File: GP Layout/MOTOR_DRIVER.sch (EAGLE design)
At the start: 46 parts, among them U2 CSD18502KCS_KCS_3, U3 MIC4604YM, U4 CSD18502KCS_KCS_3, U5 CSD18502KCS_KCS_3, U6 MIC4604YM, U7 ATMEGA328P_TQFP, Y1 16MHz

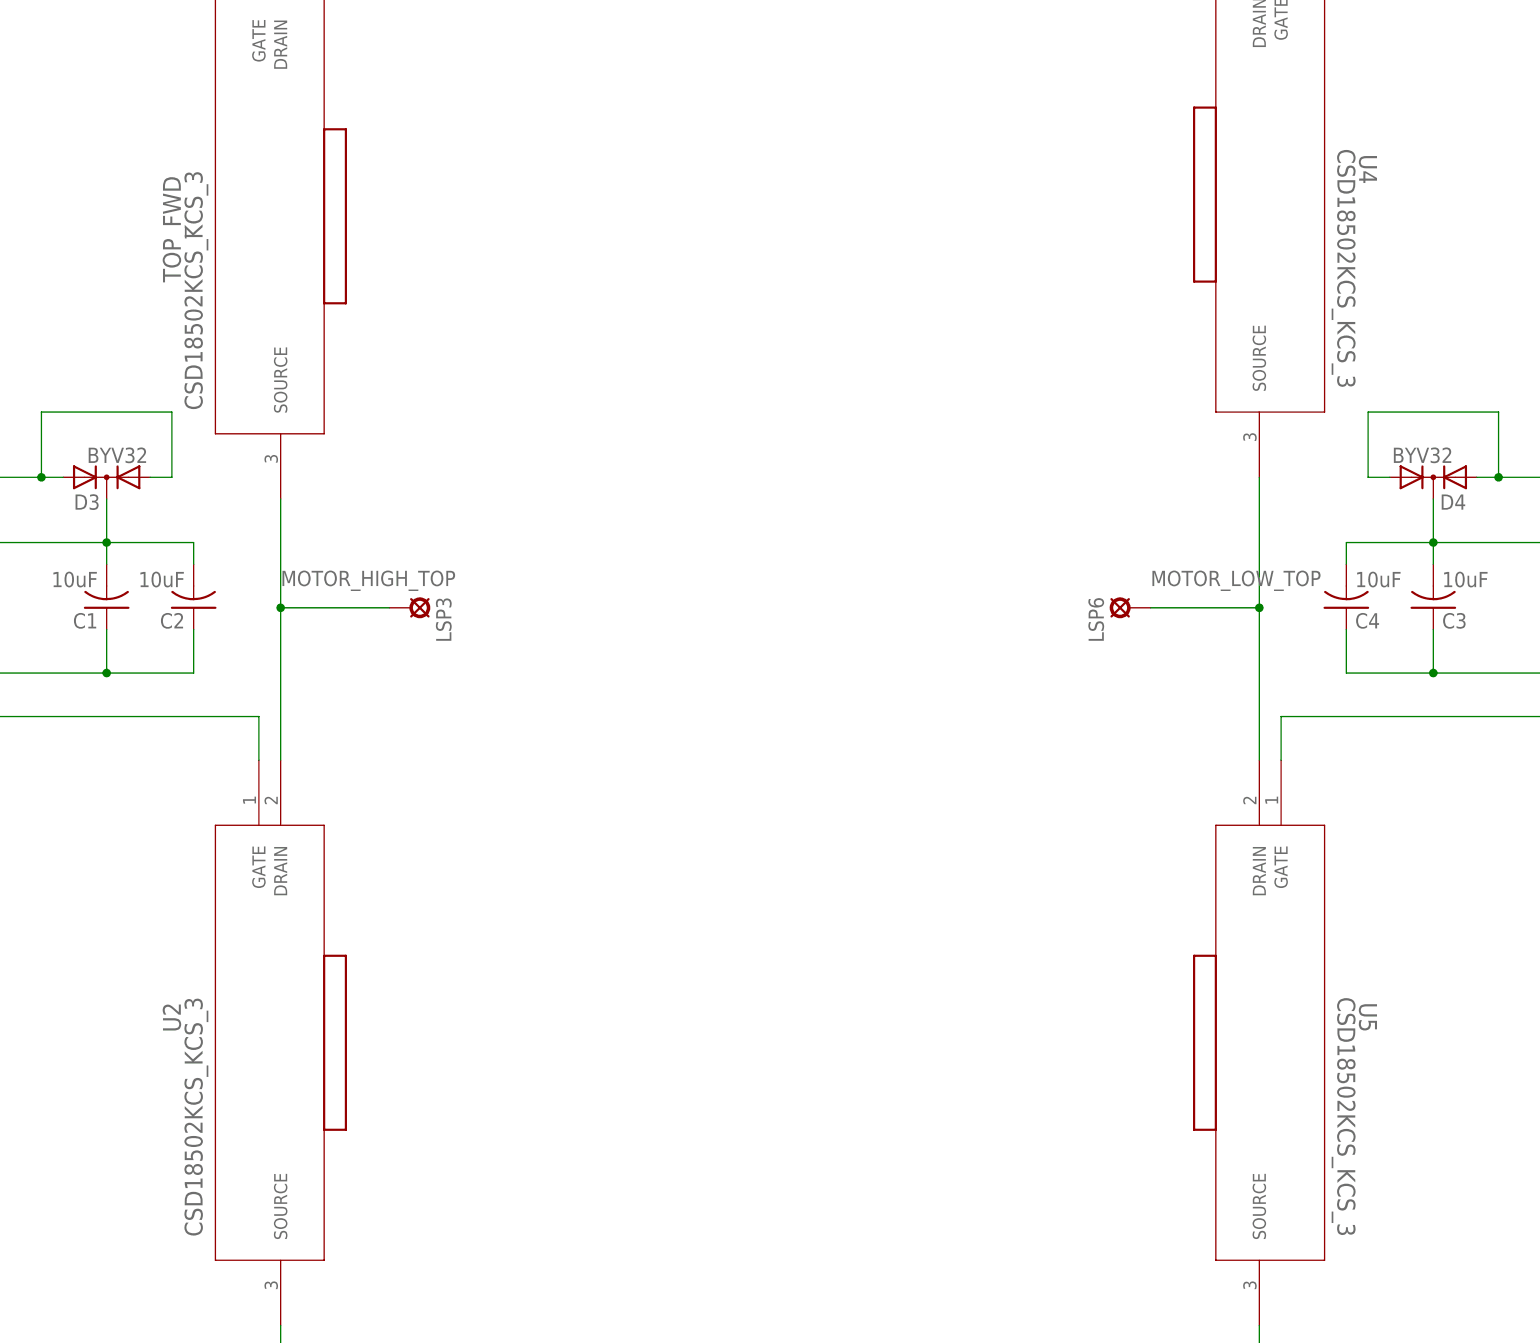
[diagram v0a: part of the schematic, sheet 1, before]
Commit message: modified footprint for MOS to have name and indicate orientation
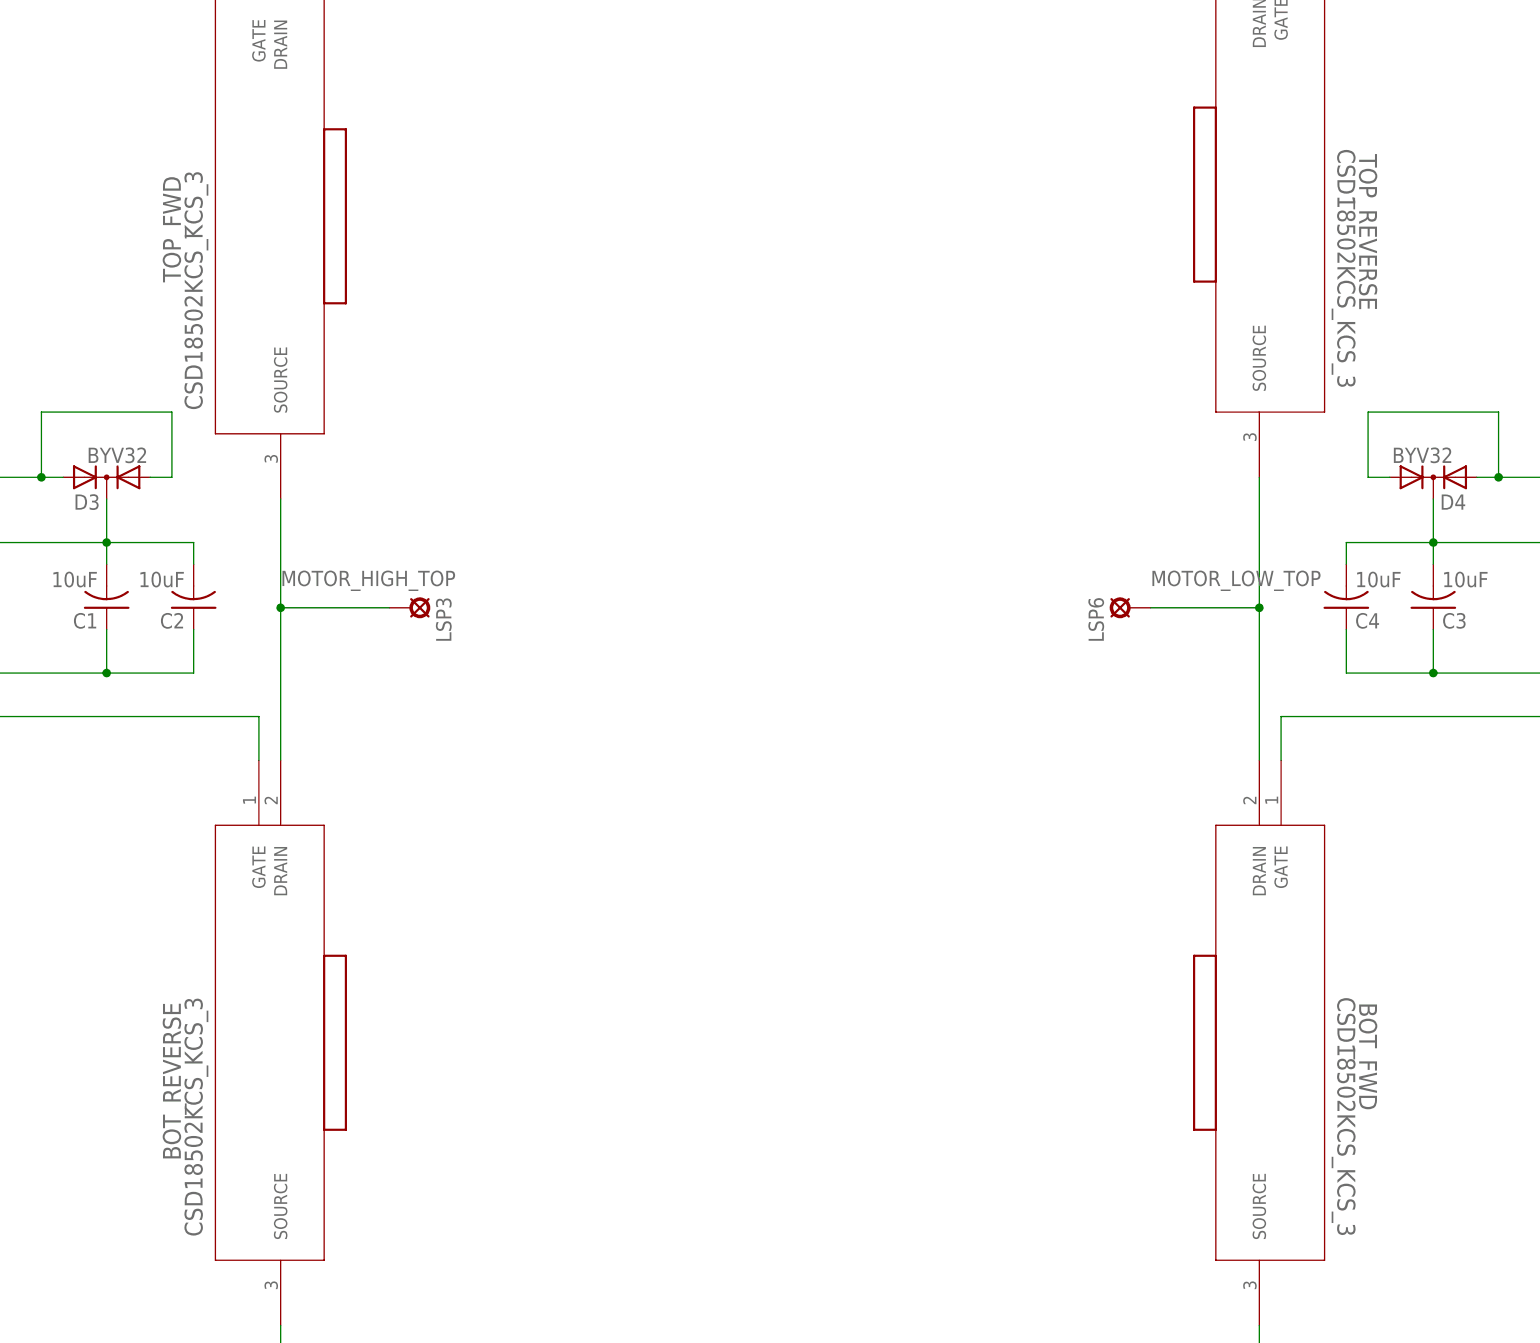
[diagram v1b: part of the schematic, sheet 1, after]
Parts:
- renumbered U2 to BOT_REVERSE, U4 to TOP_REVERSE, U5 to BOT_FWD
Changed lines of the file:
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@@
 <parts>
 <part name="TOP_FWD" library="CSD18502KCS" deviceset="CSD18502KCS_KCS_3" device=""/>
-<part name="U2" library="CSD18502KCS" deviceset="CSD18502KCS_KCS_3" device=""/>
+<part name="BOT_REVERSE" library="CSD18502KCS" deviceset="CSD18502KCS_KCS_3" device=""/>
 <part name="FRAME1" library="frames" deviceset="A3L-LOC" device=""/>
 <part name="U3" library="MIC4604" deviceset="MIC4604YM" device=""/>
@@
 <part name="C2" library="resistor" deviceset="C-US" device="025-050X050" value="10uF"/>
 <part name="LSP3" library="solpad" deviceset="SE14" device=""/>
-<part name="U4" library="CSD18502KCS" deviceset="CSD18502KCS_KCS_3" device=""/>
-<part name="U5" library="CSD18502KCS" deviceset="CSD18502KCS_KCS_3" device=""/>
+<part name="TOP_REVERSE" library="CSD18502KCS" deviceset="CSD18502KCS_KCS_3" device=""/>
+<part name="BOT_FWD" library="CSD18502KCS" deviceset="CSD18502KCS_KCS_3" device=""/>
 <part name="U6" library="MIC4604" deviceset="MIC4604YM" device=""/>
 <part name="C3" library="resistor" deviceset="C-US" device="025-050X050" value="10uF"/>
@@
 <instances>
 <instance part="TOP_FWD" gate="A" x="124.46" y="210.82" rot="MR270"/>
-<instance part="U2" gate="A" x="124.46" y="114.3" rot="MR270"/>
+<instance part="BOT_REVERSE" gate="A" x="124.46" y="114.3" rot="MR270"/>
 <instance part="FRAME1" gate="G$1" x="0" y="0"/>
 <instance part="U3" gate="A" x="86.36" y="142.24" rot="MR0"/>
@@
 <instance part="C2" gate="G$1" x="116.84" y="132.08" rot="R180"/>
 <instance part="LSP3" gate="1" x="142.24" y="132.08" rot="R270"/>
-<instance part="U4" gate="A" x="243.84" y="213.36" rot="R270"/>
-<instance part="U5" gate="A" x="243.84" y="114.3" rot="R270"/>
+<instance part="TOP_REVERSE" gate="A" x="243.84" y="213.36" rot="R270"/>
+<instance part="BOT_FWD" gate="A" x="243.84" y="114.3" rot="R270"/>
 <instance part="U6" gate="A" x="281.94" y="142.24"/>
 <instance part="C3" gate="G$1" x="261.62" y="132.08" rot="MR180"/>
@@
 <wire x1="30.48" y1="142.24" x2="15.24" y2="142.24" width="0.1524" layer="91"/>
 <wire x1="15.24" y1="142.24" x2="15.24" y2="119.38" width="0.1524" layer="91"/>
-<pinref part="U2" gate="A" pin="GATE"/>
+<pinref part="BOT_REVERSE" gate="A" pin="GATE"/>
 <wire x1="15.24" y1="119.38" x2="124.46" y2="119.38" width="0.1524" layer="91"/>
 <wire x1="124.46" y1="119.38" x2="124.46" y2="114.3" width="0.1524" layer="91"/>
@@
 <wire x1="337.82" y1="142.24" x2="353.06" y2="142.24" width="0.1524" layer="91"/>
 <wire x1="353.06" y1="142.24" x2="353.06" y2="119.38" width="0.1524" layer="91"/>
-<pinref part="U5" gate="A" pin="GATE"/>
+<pinref part="BOT_FWD" gate="A" pin="GATE"/>
 <wire x1="353.06" y1="119.38" x2="243.84" y2="119.38" width="0.1524" layer="91"/>
 <wire x1="243.84" y1="119.38" x2="243.84" y2="114.3" width="0.1524" layer="91"/>
@@
 <net name="N$10" class="0">
 <segment>
-<pinref part="U4" gate="A" pin="GATE"/>
+<pinref part="TOP_REVERSE" gate="A" pin="GATE"/>
 <wire x1="243.84" y1="213.36" x2="243.84" y2="218.44" width="0.1524" layer="91"/>
 <wire x1="243.84" y1="218.44" x2="279.4" y2="218.44" width="0.1524" layer="91"/>
@@
 <net name="GND_TOP" class="0">
 <segment>
-<pinref part="U2" gate="A" pin="SOURCE"/>
+<pinref part="BOT_REVERSE" gate="A" pin="SOURCE"/>
 <wire x1="127" y1="48.26" x2="127" y2="40.64" width="0.1524" layer="91"/>
 <pinref part="U3" gate="A" pin="VSS"/>
@@
 <wire x1="12.7" y1="40.64" x2="127" y2="40.64" width="0.1524" layer="91"/>
 <junction x="127" y="40.64"/>
-<pinref part="U5" gate="A" pin="SOURCE"/>
+<pinref part="BOT_FWD" gate="A" pin="SOURCE"/>
 <wire x1="241.3" y1="48.26" x2="241.3" y2="40.64" width="0.1524" layer="91"/>
 <pinref part="U6" gate="A" pin="VSS"/>
@@
 <junction x="127" y="220.98"/>
 <pinref part="U3" gate="A" pin="VDD"/>
-<pinref part="U4" gate="A" pin="DRAIN"/>
+<pinref part="TOP_REVERSE" gate="A" pin="DRAIN"/>
 <wire x1="86.36" y1="147.32" x2="86.36" y2="142.24" width="0.1524" layer="91"/>
 <wire x1="241.3" y1="220.98" x2="241.3" y2="213.36" width="0.1524" layer="91"/>
@@
 <segment>
 <pinref part="TOP_FWD" gate="A" pin="SOURCE"/>
-<pinref part="U2" gate="A" pin="DRAIN"/>
+<pinref part="BOT_REVERSE" gate="A" pin="DRAIN"/>
 <wire x1="127" y1="144.78" x2="127" y2="132.08" width="0.1524" layer="91"/>
 <pinref part="LSP3" gate="1" pin="MP"/>
@@
 <net name="MOTOR_LOW_TOP" class="0">
 <segment>
-<pinref part="U4" gate="A" pin="SOURCE"/>
-<pinref part="U5" gate="A" pin="DRAIN"/>
+<pinref part="TOP_REVERSE" gate="A" pin="SOURCE"/>
+<pinref part="BOT_FWD" gate="A" pin="DRAIN"/>
 <wire x1="241.3" y1="147.32" x2="241.3" y2="132.08" width="0.1524" layer="91"/>
 <pinref part="LSP6" gate="1" pin="MP"/>

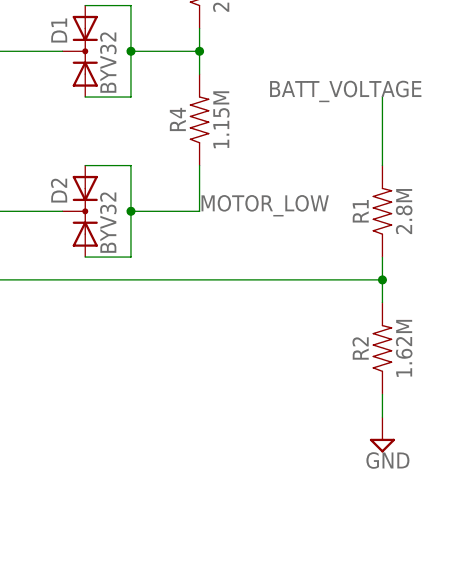
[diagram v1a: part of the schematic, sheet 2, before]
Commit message: Changed battery sense resistances
Input impedance might be too high for the Teensy ADC
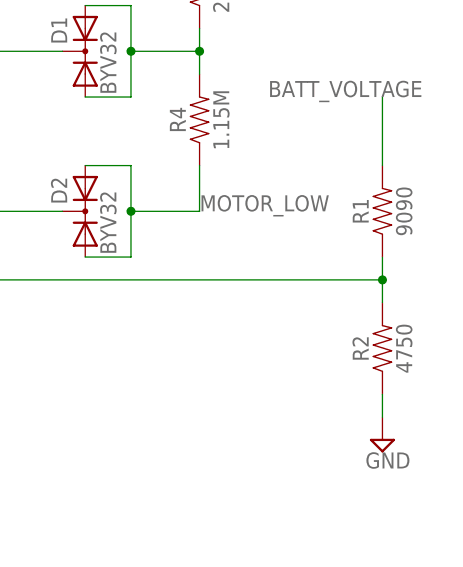
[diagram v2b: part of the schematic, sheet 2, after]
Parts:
- R1: value 2.8M -> 9090
- R2: value 1.62M -> 4750
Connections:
- net 5V: now also SV1.8
- net GND: now also SV1.10
- net SERVO: now also SV1.9
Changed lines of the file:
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@@
 <?xml version="1.0" encoding="utf-8"?>
 <!DOCTYPE eagle SYSTEM "eagle.dtd">
-<eagle version="8.0.1">
+<eagle version="8.0.0">
 <drawing>
 <settings>
@@
 <part name="FUSE" library="minifuse" deviceset="FUSEHOLDER3588" device=""/>
 <part name="BIG_SWITCH" library="bigswitch" deviceset="BIGSWITCH" device=""/>
-<part name="R1" library="SparkFun-Resistors" deviceset="0.3OHM" device="-0805-1/8W-1%" value="2.8M"/>
-<part name="R2" library="SparkFun-Resistors" deviceset="0.3OHM" device="-0805-1/8W-1%" value="1.62M"/>
+<part name="R1" library="SparkFun-Resistors" deviceset="0.3OHM" device="-0805-1/8W-1%" value="9090"/>
+<part name="R2" library="SparkFun-Resistors" deviceset="0.3OHM" device="-0805-1/8W-1%" value="4750"/>
 <part name="SUPPLY2" library="supply2" deviceset="GND" device=""/>
 <part name="R3" library="SparkFun-Resistors" deviceset="0.3OHM" device="-0805-1/8W-1%" value="2.32M"/>
@@
 <wire x1="55.88" y1="157.48" x2="81.28" y2="157.48" width="0.1524" layer="91"/>
 <label x="76.2" y="157.48" size="1.778" layer="95"/>
+<pinref part="SV1" gate="G$1" pin="10"/>
 </segment>
 <segment>
@@
 <wire x1="55.88" y1="152.4" x2="81.28" y2="152.4" width="0.1524" layer="91"/>
 <label x="76.2" y="152.4" size="1.778" layer="95"/>
+<pinref part="SV1" gate="G$1" pin="8"/>
 </segment>
 <segment>
@@
 <wire x1="55.88" y1="154.94" x2="81.28" y2="154.94" width="0.1524" layer="91"/>
 <label x="73.66" y="154.94" size="1.778" layer="95"/>
-</segment>
-</net>
+<pinref part="SV1" gate="G$1" pin="9"/>
+</segment>
+</net>

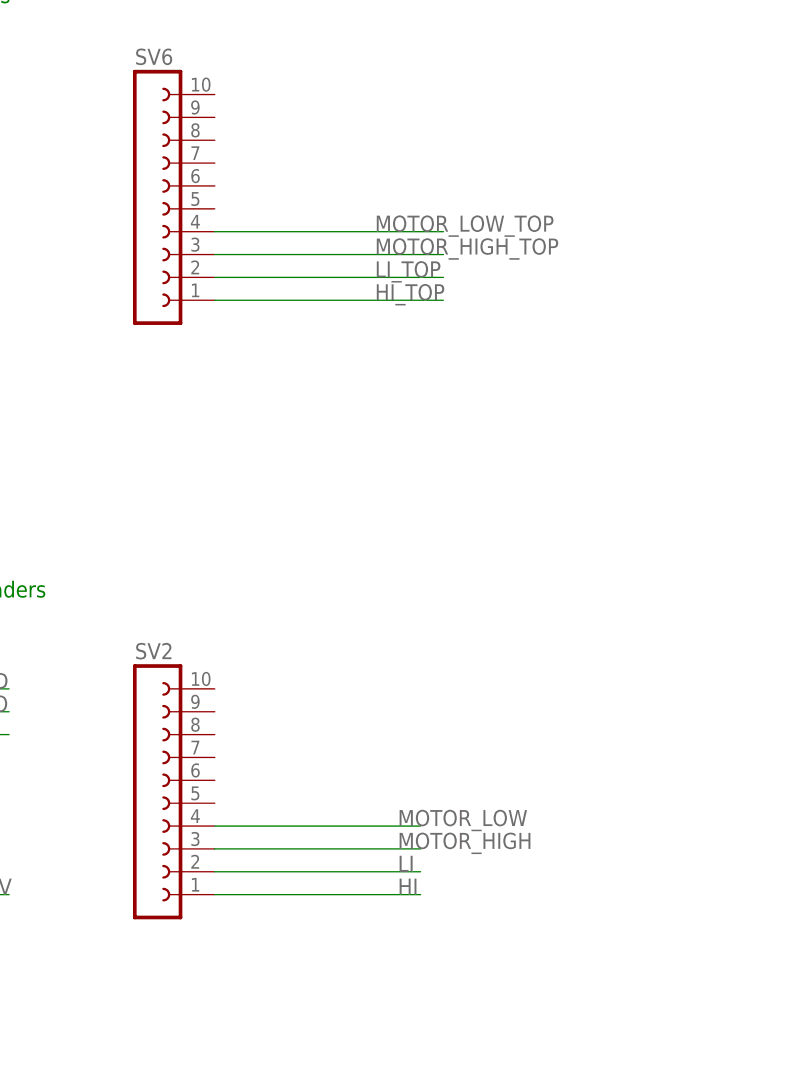
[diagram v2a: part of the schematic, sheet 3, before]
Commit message: added motor inputs for full bridge
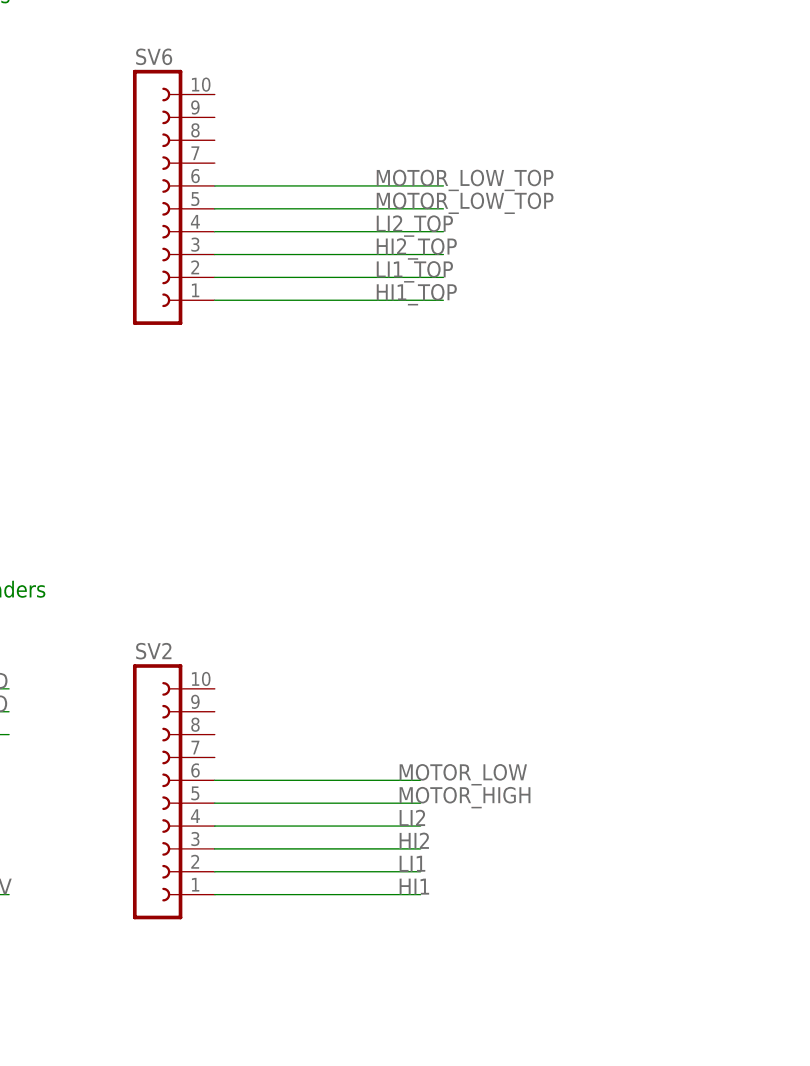
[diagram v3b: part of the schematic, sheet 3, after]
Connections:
- net HI renamed HI1
- net LI renamed LI1
- new net HI1_TOP: SV6.1, U3.HI
- new net HI2: SV2.3, U$1.5
- new net HI2_TOP: SV6.3
- new net LI1_TOP: SV6.2, U3.LI
- new net LI2: SV2.4, U$1.6
- new net LI2_TOP: SV6.4
- net HI_TOP: no longer SV6.1, U3.HI
- net LI_TOP: no longer SV6.2, U3.LI
- net MOTOR_HIGH: now also SV2.5; no longer SV2.3
- net MOTOR_HIGH_TOP: no longer SV6.3
- net MOTOR_LOW: now also SV2.6; no longer SV2.4
- net MOTOR_LOW_TOP: now also SV6.5, SV6.6; no longer SV6.4

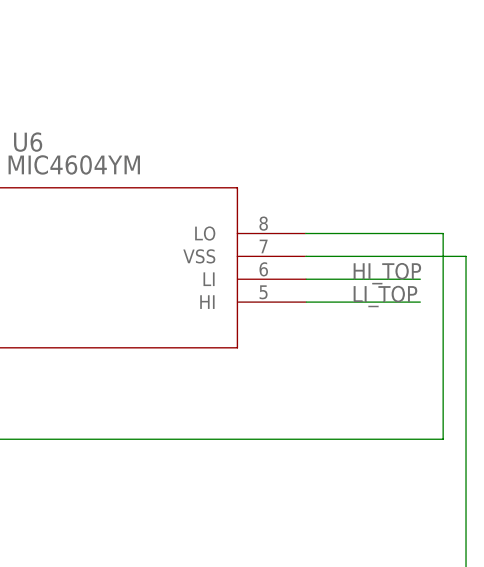
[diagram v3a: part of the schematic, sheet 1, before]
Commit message: fixed LI2 and HI2 errors
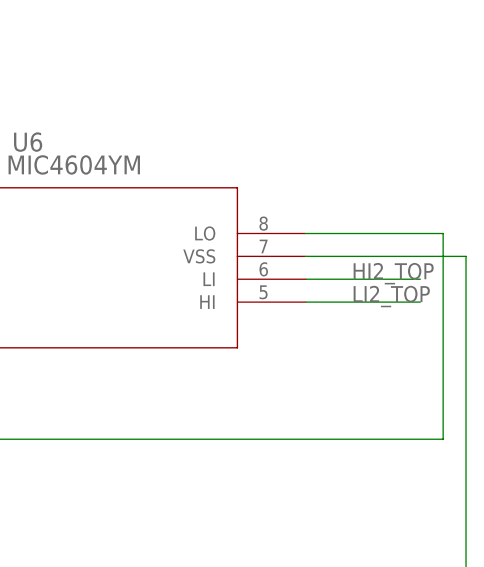
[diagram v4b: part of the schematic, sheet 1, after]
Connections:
- removed net HI_TOP: U6.LI
- removed net LI_TOP: U6.HI
- net HI2_TOP: now also U6.LI
- net LI2_TOP: now also U6.HI
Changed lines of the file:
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@@
 </segment>
 </net>
-<net name="LI_TOP" class="0">
+<net name="LI2_TOP" class="0">
 <segment>
 <pinref part="U6" gate="A" pin="HI"/>
@@
 </segment>
 </net>
-<net name="HI_TOP" class="0">
+<net name="HI2_TOP" class="0">
 <segment>
 <pinref part="U6" gate="A" pin="LI"/>
